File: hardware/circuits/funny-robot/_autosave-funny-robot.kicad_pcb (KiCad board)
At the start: 2 copper layers, 69.5 x 99 mm, 10 parts, among them J1 To SSD1306OLED, J2 I2C Jumper, U1 Tiny_RTC_DS1307, U2 pca9685 module

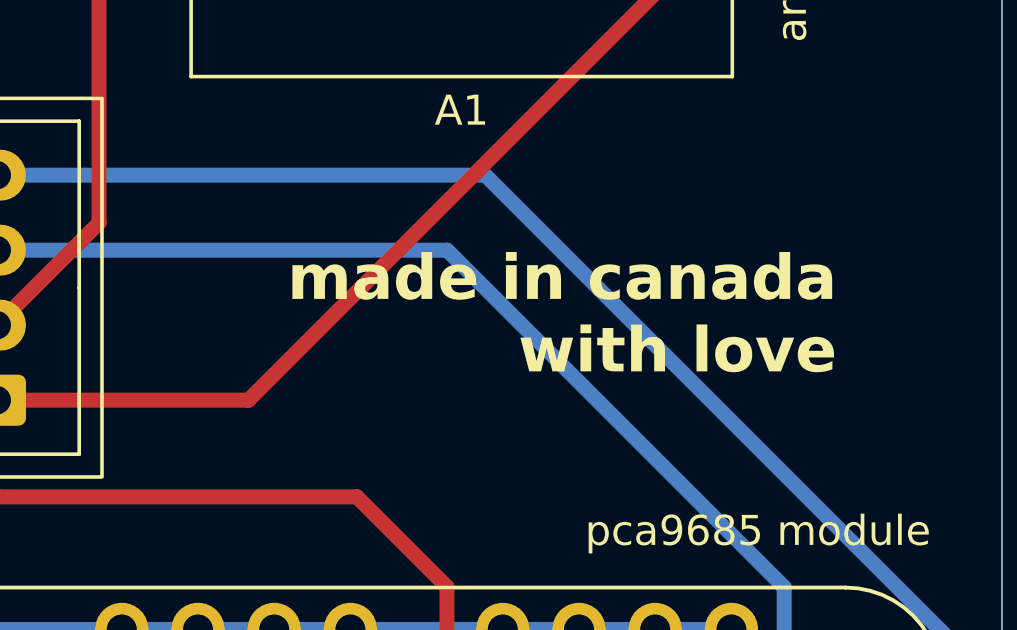
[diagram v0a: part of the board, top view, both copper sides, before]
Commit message: Updated PCB to comply with customs
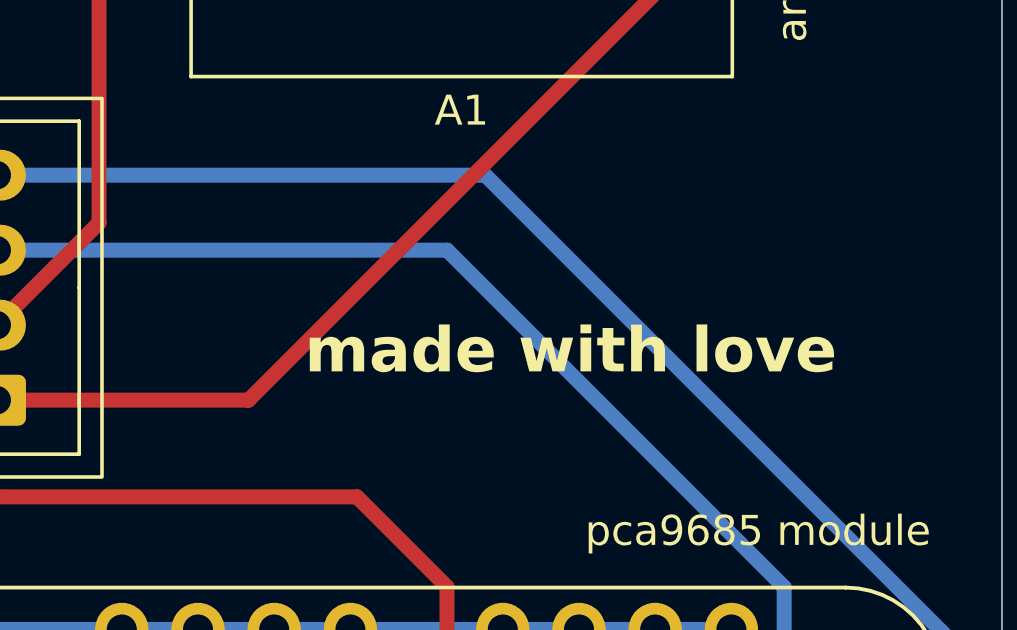
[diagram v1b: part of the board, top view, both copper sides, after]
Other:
- board text added: "made with love"
- board text removed: "made in canada with love"
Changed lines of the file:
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@@
 		)
 	)
-	(gr_text "made in canada\nwith love"
+	(gr_text "made with love"
 		(at 174.5 102.5 0)
 		(layer "F.SilkS")
